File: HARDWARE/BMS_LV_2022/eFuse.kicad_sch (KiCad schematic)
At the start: 14 parts, among them Q10 BSS138, Q11 SiSS05DN, Q12 SiSS05DN, Q8 SiSS05DN, Q9 SiSS05DN

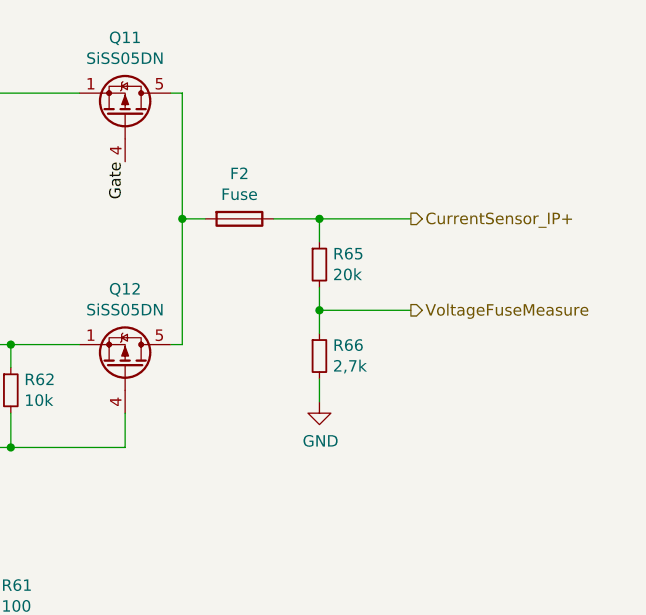
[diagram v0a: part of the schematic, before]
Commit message: New fuses and programming connector added
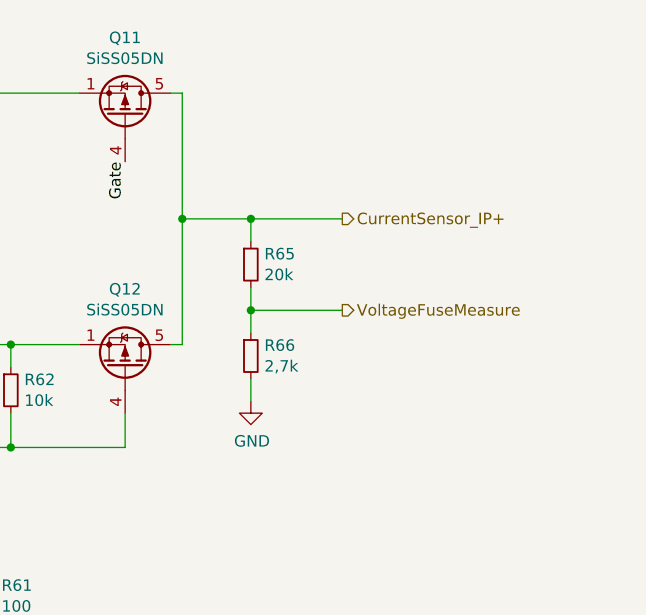
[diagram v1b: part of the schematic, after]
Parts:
- removed F2: Fuse, footprints:3557-2, symbol Device:Fuse
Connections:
- net CurrentSensor_IP+: now also Q11.5 (D), Q12.5 (D)
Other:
- moved on the sheet: R65, R66
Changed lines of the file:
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@@
-	)
-	(junction
-		(at 187.96 71.12)
-		(diameter 0)
-		(color 0 0 0 0)
 	)
 	(junction
@@
 	)
 	(junction
-		(at 187.96 81.28)
+		(at 180.34 81.28)
 		(diameter 0)
 		(color 0 0 0 0)
@@
 	)
 	(junction
+		(at 180.34 71.12)
+		(diameter 0)
+		(color 0 0 0 0)
+	)
+	(junction
 		(at 151.13 57.15)
 		(diameter 0)
@@
 	(wire
 		(pts
-			(xy 187.96 71.12) (xy 198.12 71.12)
+			(xy 180.34 71.12) (xy 190.5 71.12)
 		)
 		(stroke
@@
 	(wire
 		(pts
-			(xy 187.96 88.9) (xy 187.96 91.44)
+			(xy 180.34 88.9) (xy 180.34 91.44)
 		)
 		(stroke
@@
 	(wire
 		(pts
-			(xy 187.96 81.28) (xy 187.96 83.82)
-		)
-		(stroke
-			(width 0)
-			(type default)
-		)
-	)
-	(wire
-		(pts
-			(xy 187.96 78.74) (xy 187.96 81.28)
+			(xy 180.34 81.28) (xy 180.34 83.82)
+		)
+		(stroke
+			(width 0)
+			(type default)
+		)
+	)
+	(wire
+		(pts
+			(xy 180.34 78.74) (xy 180.34 81.28)
 		)
 		(stroke
@@
 	(wire
 		(pts
-			(xy 182.88 71.12) (xy 187.96 71.12)
-		)
-		(stroke
-			(width 0)
-			(type default)
-		)
-	)
-	(wire
-		(pts
 			(xy 135.89 96.52) (xy 148.59 96.52)
 		)
@@
 	(wire
 		(pts
+			(xy 172.72 71.12) (xy 180.34 71.12)
+		)
+		(stroke
+			(width 0)
+			(type default)
+		)
+	)
+	(wire
+		(pts
 			(xy 140.97 130.81) (xy 142.24 130.81)
 		)
@@
 	(wire
 		(pts
-			(xy 187.96 73.66) (xy 187.96 71.12)
-		)
-		(stroke
-			(width 0)
-			(type default)
-		)
-	)
-	(wire
-		(pts
-			(xy 187.96 81.28) (xy 198.12 81.28)
+			(xy 180.34 73.66) (xy 180.34 71.12)
+		)
+		(stroke
+			(width 0)
+			(type default)
+		)
+	)
+	(wire
+		(pts
+			(xy 180.34 81.28) (xy 190.5 81.28)
 		)
 		(stroke
@@
 		(pts
 			(xy 129.54 71.12) (xy 129.54 85.09)
-		)
-		(stroke
-			(width 0)
-			(type default)
-		)
-	)
-	(wire
-		(pts
-			(xy 172.72 71.12) (xy 175.26 71.12)
 		)
 		(stroke
@@
 	(label "Gate"
 		(at 166.37 64.77 270)
+		(fields_autoplaced yes)
 		(effects
 			(font
@@
 	(label "Gate"
 		(at 151.13 101.6 270)
+		(fields_autoplaced yes)
 		(effects
 			(font
@@
 	(label "Gate"
 		(at 135.89 64.77 270)
+		(fields_autoplaced yes)
 		(effects
 			(font
@@
 		(shape output)
 		(at 123.19 57.15 90)
+		(fields_autoplaced yes)
 		(effects
 			(font
@@
 	(hierarchical_label "VoltageFuseMeasure"
 		(shape output)
-		(at 198.12 81.28 0)
+		(at 190.5 81.28 0)
+		(fields_autoplaced yes)
 		(effects
 			(font
@@
 	(hierarchical_label "CurrentSensor_IP+"
 		(shape output)
-		(at 198.12 71.12 0)
+		(at 190.5 71.12 0)
+		(fields_autoplaced yes)
 		(effects
 			(font
@@
 		(shape input)
 		(at 130.81 124.46 180)
+		(fields_autoplaced yes)
 		(effects
 			(font
@@
 					(unit 1)
 				)
-				(path "/fb6504b5-591d-4b10-ab86-0c46f59e8b7d"
-					(reference "Q8")
-					(unit 1)
-				)
 			)
 		)
@@
 			(project "BMS_LV_2022"
 				(path "/fb6504b5-591d-4b10-ab86-0c46f59e8b7d/00000000-0000-0000-0000-00006269845f"
-					(reference "Q9")
-					(unit 1)
-				)
-				(path "/fb6504b5-591d-4b10-ab86-0c46f59e8b7d"
 					(reference "Q9")
 					(unit 1)
@@
 					(unit 1)
 				)
-				(path "/fb6504b5-591d-4b10-ab86-0c46f59e8b7d"
-					(reference "Q11")
-					(unit 1)
-				)
 			)
 		)
@@
 					(unit 1)
 				)
-				(path "/fb6504b5-591d-4b10-ab86-0c46f59e8b7d"
-					(reference "Q12")
-					(unit 1)
-				)
 			)
 		)
@@
 	(symbol
 		(lib_id "Device:R_Small")
-		(at 187.96 76.2 0)
+		(at 180.34 76.2 0)
 		(unit 1)
 		(exclude_from_sim no)
@@
 		(dnp no)
 		(property "Reference" "R65"
-			(at 189.4586 75.0316 0)
+			(at 181.8386 75.0316 0)
 			(effects
 				(font
@@
 		)
 		(property "Value" "20k"
-			(at 189.4586 77.343 0)
+			(at 181.8386 77.343 0)
 			(effects
 				(font
@@
 		)
 		(property "Footprint" "Resistor_SMD:R_0603_1608Metric"
-			(at 187.96 76.2 0)
+			(at 180.34 76.2 0)
 			(effects
 				(font
@@
 		)
 		(property "Datasheet" "~"
-			(at 187.96 76.2 0)
+			(at 180.34 76.2 0)
 			(effects
 				(font
@@
 		)
 		(property "Description" ""
-			(at 187.96 76.2 0)
+			(at 180.34 76.2 0)
 			(effects
 				(font
@@
 	(symbol
 		(lib_id "Device:R_Small")
-		(at 187.96 86.36 0)
+		(at 180.34 86.36 0)
 		(unit 1)
 		(exclude_from_sim no)
@@
 		(dnp no)
 		(property "Reference" "R66"
-			(at 189.4586 85.1916 0)
+			(at 181.8386 85.1916 0)
 			(effects
 				(font
@@
 		)
 		(property "Value" "2,7k"
-			(at 189.4586 87.503 0)
+			(at 181.8386 87.503 0)
 			(effects
 				(font
@@
 		)
 		(property "Footprint" "Resistor_SMD:R_0603_1608Metric"
-			(at 187.96 86.36 0)
+			(at 180.34 86.36 0)
 			(effects
 				(font
@@
 		)
 		(property "Datasheet" "~"
-			(at 187.96 86.36 0)
+			(at 180.34 86.36 0)
 			(effects
 				(font
@@
 		)
 		(property "Description" ""
-			(at 187.96 86.36 0)
+			(at 180.34 86.36 0)
 			(effects
 				(font
@@
 	(symbol
 		(lib_id "BMS_LV_2022-rescue:GND-power")
-		(at 187.96 91.44 0)
+		(at 180.34 91.44 0)
 		(unit 1)
 		(exclude_from_sim no)
@@
 		(dnp no)
 		(property "Reference" "#PWR0101"
-			(at 187.96 97.79 0)
+			(at 180.34 97.79 0)
 			(effects
 				(font
@@
 		)
 		(property "Value" "GND"
-			(at 188.087 95.8342 0)
+			(at 180.467 95.8342 0)
 			(effects
 				(font
@@
 		)
 		(property "Footprint" ""
-			(at 187.96 91.44 0)
+			(at 180.34 91.44 0)
 			(effects
 				(font
@@
 		)
 		(property "Datasheet" ""
-			(at 187.96 91.44 0)
+			(at 180.34 91.44 0)
 			(effects
 				(font
@@
 		)
 		(property "Description" ""
-			(at 187.96 91.44 0)
+			(at 180.34 91.44 0)
 			(effects
 				(font
@@
 				(path "/fb6504b5-591d-4b10-ab86-0c46f59e8b7d/00000000-0000-0000-0000-00006269845f"
 					(reference "#PWR0101")
-					(unit 1)
-				)
-				(path "/fb6504b5-591d-4b10-ab86-0c46f59e8b7d"
-					(reference "#PWR?")
 					(unit 1)
 				)
@@
 					(unit 1)
 				)
-				(path "/fb6504b5-591d-4b10-ab86-0c46f59e8b7d"
-					(reference "#PWR?")
-					(unit 1)
-				)
 			)
 		)
@@
 					(unit 1)
 				)
-				(path "/fb6504b5-591d-4b10-ab86-0c46f59e8b7d"
-					(reference "#PWR?")
-					(unit 1)
-				)
 			)
 		)
@@
 					(unit 1)
 				)
-				(path "/fb6504b5-591d-4b10-ab86-0c46f59e8b7d"
-					(reference "Q?")
-					(unit 1)
-				)
 			)
 		)
@@
 					(unit 1)
 				)
-				(path "/fb6504b5-591d-4b10-ab86-0c46f59e8b7d"
-					(reference "R?")
-					(unit 1)
-				)
 			)
 		)
@@
 				(path "/fb6504b5-591d-4b10-ab86-0c46f59e8b7d/00000000-0000-0000-0000-00006269845f"
 					(reference "R60")
-					(unit 1)
-				)
-				(path "/fb6504b5-591d-4b10-ab86-0c46f59e8b7d"
-					(reference "R?")
 					(unit 1)
 				)
@@
 					(unit 1)
 				)
-			)
-		)
-	)
-	(symbol
-		(lib_id "Device:Fuse")
-		(at 179.07 71.12 270)
-		(unit 1)
-		(exclude_from_sim no)
-		(in_bom yes)
-		(on_board yes)
-		(dnp no)
-		(property "Reference" "F2"
-			(at 179.07 66.1162 90)
-			(effects
-				(font
-					(size 1.27 1.27)
-				)
-			)
-		)
-		(property "Value" "Fuse"
-			(at 179.07 68.4276 90)
-			(effects
-				(font
-					(size 1.27 1.27)
-				)
-			)
-		)
-		(property "Footprint" "footprints:3557-2"
-			(at 179.07 69.342 90)
-			(effects
-				(font
-					(size 1.27 1.27)
-				)
-				(hide yes)
-			)
-		)
-		(property "Datasheet" "~"
-			(at 179.07 71.12 0)
-			(effects
-				(font
-					(size 1.27 1.27)
-				)
-				(hide yes)
-			)
-		)
-		(property "Description" ""
-			(at 179.07 71.12 0)
-			(effects
-				(font
-					(size 1.27 1.27)
-				)
-				(hide yes)
-			)
-		)
-		(property "Part Number" "3557-2"
-			(at 179.07 71.12 0)
-			(effects
-				(font
-					(size 1.27 1.27)
-				)
-				(hide yes)
-			)
-		)
-		(pin "2"
-		)
-		(pin "1"
-		)
-		(instances
-			(project "BMS_LV_2022"
-				(path "/fb6504b5-591d-4b10-ab86-0c46f59e8b7d/00000000-0000-0000-0000-00006269845f"
-					(reference "F2")
-					(unit 1)
-				)

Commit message: Significant changes
-main connector changed to the other side of the pcb because of using socket connector in the new version
-changed usb mini to usb-c
-changed fuse to 2 fuses protecting current path pins separately
-some minor changes in layout
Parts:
- R66: value 2,7k -> 2.7k
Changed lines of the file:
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@@
 			)
 		)
-		(property "Value" "2,7k"
+		(property "Value" "2.7k"
 			(at 181.8386 87.503 0)
 			(effects
